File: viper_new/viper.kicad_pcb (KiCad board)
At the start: 2 copper layers, 285 x 95.1 mm, 272 parts, among them SW1 SW_Push, SW10 SW_Push, SW11 SW_Push, SW12 SW_Push, SW13 SW_Push, SW14 SW_Push, SW14_1 SW_Push, SW15 SW_Push, SW16 SW_Push, SW17 SW_Push, SW18 SW_Push, SW19 SW_Push, SW2 SW_Push, SW20 SW_Push, SW21 SW_Push, SW22 SW_Push, SW23 SW_Push, SW24 SW_Push, SW25 SW_Push, SW26 SW_Push, SW27 SW_Push, SW28 SW_Push, SW28_1 SW_Push, SW29 SW_Push, SW29_1 SW_Push, SW3 SW_Push, SW30 SW_Push, SW31 SW_Push, SW32 SW_Push, SW33 SW_Push, SW34 SW_Push, SW35 SW_Push, SW36 SW_Push, SW37 SW_Push, SW38 SW_Push, SW39 SW_Push, SW4 SW_Push, SW40 SW_Push, SW41 SW_Push, SW41_1 SW_Push, SW42 SW_Push, SW43 SW_Push, SW43_1 SW_Push, SW44 SW_Push, SW45 SW_Push, SW46 SW_Push, SW47 SW_Push, SW48 SW_Push, SW49 SW_Push, SW5 SW_Push, SW50 SW_Push, SW51 SW_Push, SW52 SW_Push, SW53 SW_Push, SW54 SW_Push, SW55 SW_Push, SW55_1 SW_Push, SW56 SW_Push, SW57 SW_Push, SW58 SW_Push, SW59 SW_Push, SW6 SW_Push, SW60 SW_Push, SW61 SW_Push, SW7 SW_Push, SW8 SW_Push, SW9 SW_Push

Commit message: YAKE - YET ANOTHER KEYBOARD EXPORT
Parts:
- D1, D10, D11, D12, D13, D14, D15, D16, D17, D18, D19, D2, D20, D21, D22, D23, D24, D25, D26, D27, D28, D29, D3, D30, D31, D32, D33, D34, D35, D36, D37, D38, D39, D4, D40, D41, D42, D43, D44, D45, D46, D47, D48, D49, D5, D50, D51, D52, D53, D54, D55, D56, D57, D58, D59, D6, D60, D61, D7, D8, D9: footprint Diode_SMD:D_SOD-123 -> Diode_SMD:D_SOD-123F
- H1: value Center Oval Mounting Hole -> Mid Viper Oval Mounting Hole; footprint acheron_MountingHoles:MoutingHole_Oval_7mm_5.0x2.5mm -> acheron_MountingHoles:Mounting_Hole_Oval_2.5x8mm
- H2: value Oval Mounting Hole -> \ Oval Mounting Hole
- H3: value Oval Mounting Hole -> Tab Oval Mounting Hole
- H4: value Mounting Hole -> G-H Mounting Hole; footprint acheron_MountingHoles:MountingHole_2.5x5.0mm -> acheron_MountingHoles:MoutingHole_Oval_BackOnly_7mm_5.0x2.5mm
- H5: value Half Side Hole -> Left Edge Half Side Hole
- H6: value Half Side Hole -> Right Edge Half Side Hole
- H7: value Oval Mounting Hole -> Space Bar Oval Mounting Hole
- H8: value Bottom Half Side Hole -> Left Bottom Half Side Hole
- H9: value Bottom Half Side Hole -> Right Bottom Half Side Hole
- R1, R10, R11, R12, R13, R14, R15, R16, R17, R18, R19, R2, R20, R21, R22, R23, R24, R25, R26, R27, R28, R29, R3, R30, R31, R32, R33, R34, R35, R36, R37, R38, R39, R4, R40, R41, R42, R43, R44, R45, R46, R47, R48, R49, R5, R50, R51, R52, R53, R54, R55, R56, R57, R58, R59, R6, R60, R61, R7, R8, R9: moved to B.Cu
- SW1, SW10, SW11, SW12, SW13, SW14_1, SW16, SW17, SW18, SW19, SW2, SW20, SW21, SW22, SW23, SW24, SW25, SW26, SW27, SW28_1, SW3, SW30, SW31, SW32, SW33, SW34, SW35, SW36, SW37, SW38, SW39, SW4, SW40, SW41_1, SW42, SW44, SW45, SW46, SW47, SW48, SW49, SW5, SW50, SW51, SW52, SW53, SW54, SW56, SW57, SW6, SW61, SW7, SW8, SW9: footprint PCM_Switch_Keyboard_Cherry_MX:SW_Cherry_MX_PCB_1.00u -> PCM_Switch_Keyboard_Hybrid:SW_Hybrid_Cherry_MX_Alps_1.00u
- SW14: footprint PCM_Switch_Keyboard_Cherry_MX:SW_Cherry_MX_PCB_1.00u -> PCM_Switch_Keyboard_Hybrid:SW_Hybrid_Cherry_MX_Alps_2.00u
- SW15, SW28, SW58, SW60: footprint PCM_Switch_Keyboard_Cherry_MX:SW_Cherry_MX_PCB_1.00u -> PCM_Switch_Keyboard_Hybrid:SW_Hybrid_Cherry_MX_Alps_1.50u
- SW29, SW55_1: footprint PCM_Switch_Keyboard_Cherry_MX:SW_Cherry_MX_PCB_1.00u -> PCM_Switch_Keyboard_Hybrid:SW_Hybrid_Cherry_MX_Alps_1.75u
- SW29_1, SW43_1: footprint PCM_Switch_Keyboard_Cherry_MX:SW_Cherry_MX_PCB_1.00u -> PCM_Switch_Keyboard_Hybrid:SW_Hybrid_Cherry_MX_Alps_1.25u
- SW41, SW43: footprint PCM_Switch_Keyboard_Cherry_MX:SW_Cherry_MX_PCB_1.00u -> PCM_Switch_Keyboard_Hybrid:SW_Hybrid_Cherry_MX_Alps_2.25u
- SW55: footprint PCM_Switch_Keyboard_Cherry_MX:SW_Cherry_MX_PCB_1.00u -> PCM_Switch_Keyboard_Hybrid:SW_Hybrid_Cherry_MX_Alps_2.75u
- SW59: footprint PCM_Switch_Keyboard_Cherry_MX:SW_Cherry_MX_PCB_1.00u -> PCM_Switch_Keyboard_Hybrid:SW_Hybrid_Cherry_MX_Alps_7.00u
- moved D25 6.23 mm to (295.3, 64.8), turned to 0 degrees
- moved D40 6.23 mm to (319.1, 83.8), turned to 0 degrees
- moved D52 6.23 mm to (271.5, 102.8), turned to 0 degrees
- moved D58 6.23 mm to (147.6, 121.9), turned to 0 degrees
- moved D59 6.23 mm to (228.6, 121.9), turned to 0 degrees
- moved D17 6.23 mm to (142.9, 64.8), turned to 0 degrees
- moved D19 6.23 mm to (181.0, 64.8), turned to 0 degrees
- moved D21 6.23 mm to (219.1, 64.8), turned to 0 degrees
- moved D22 6.23 mm to (238.1, 64.8), turned to 0 degrees
- moved D3 6.23 mm to (133.3, 45.7), turned to 0 degrees
- moved D5 6.23 mm to (171.4, 45.7), turned to 0 degrees
- moved D6 6.23 mm to (190.5, 45.7), turned to 0 degrees
- moved D8 6.23 mm to (228.6, 45.7), turned to 0 degrees
- moved D31 6.23 mm to (147.6, 83.8), turned to 0 degrees
- moved D32 6.23 mm to (166.7, 83.8), turned to 0 degrees
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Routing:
- net COL11: track 0.00 -> 118.5 mm
- net COL0: track 0.00 -> 102.0 mm
- net COL10: track 0.00 -> 82.2 mm
- net COL6: track 0.00 -> 82.2 mm
- net COL4: track 0.00 -> 82.2 mm
- net COL9: track 0.00 -> 82.2 mm
- net COL5: track 0.00 -> 82.2 mm
- net COL8: track 0.00 -> 82.2 mm
- net COL3: track 0.00 -> 82.2 mm
- net COL7: track 0.00 -> 82.2 mm
- net COL2: track 0.00 -> 82.2 mm
- net COL1: track 0.00 -> 80.4 mm
- net COL12: track 0.00 -> 57.9 mm
- net ROW2: track 0.00 -> 46.8 mm
- net COL13: track 0.00 -> 35.3 mm
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
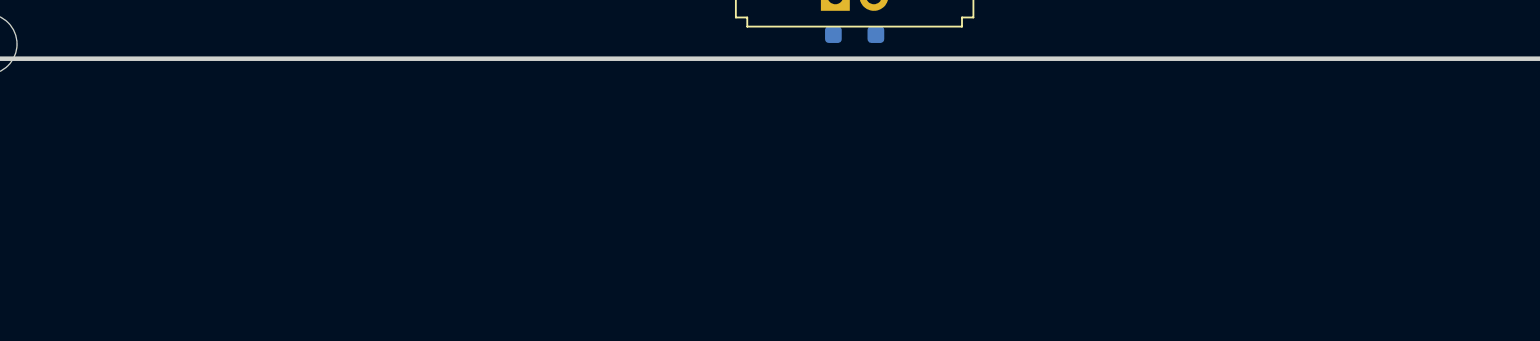
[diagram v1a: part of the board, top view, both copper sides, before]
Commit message: Added LED matrix & RGB LEDs
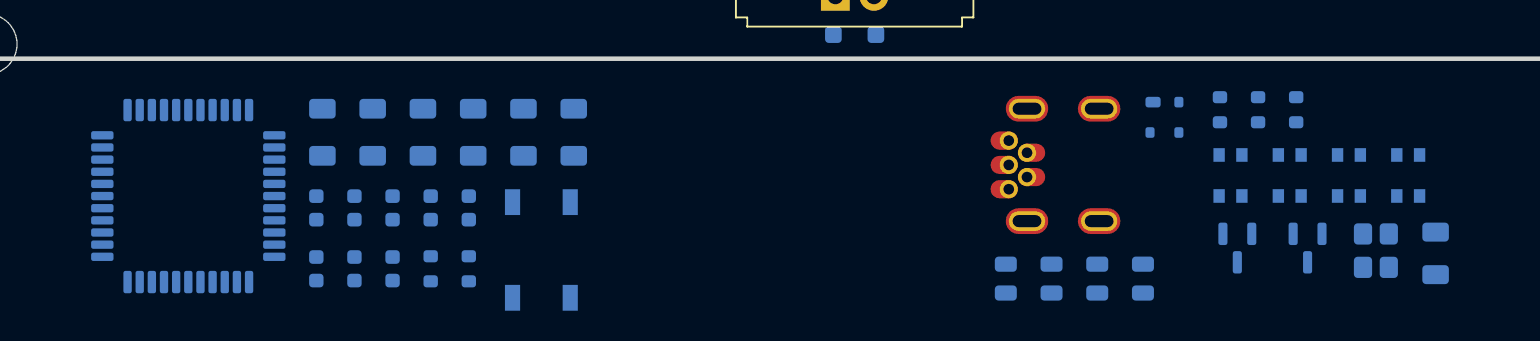
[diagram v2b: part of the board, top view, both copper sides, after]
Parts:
- added C1: 22p, Capacitor_SMD:C_0603_1608Metric, B.Cu at (193.2, 133.3)
- added C2: 22p, Capacitor_SMD:C_0603_1608Metric, B.Cu at (195.7, 133.3)
- added C3: 0.1u, Capacitor_SMD:C_0603_1608Metric, B.Cu at (198.2, 133.3)
- added C4: 0.1u, Capacitor_SMD:C_0603_1608Metric, B.Cu at (200.7, 133.3)
- added C5: 0.1u, Capacitor_SMD:C_0603_1608Metric, B.Cu at (203.2, 133.3)
- added C6: 0.1u, Capacitor_SMD:C_0603_1608Metric, B.Cu at (193.2, 137.3)
- added C7: 10u, Capacitor_SMD:C_0603_1608Metric, B.Cu at (195.7, 137.3)
- added C8: 1u, Capacitor_SMD:C_0603_1608Metric, B.Cu at (198.2, 137.3)
- added CRGB1: 100n, Capacitor_SMD:C_0805_2012Metric, B.Cu at (238.6, 138.0)
- added CRGB10: 100n, Capacitor_SMD:C_0805_2012Metric, B.Cu at (247.6, 138.0)
- added CRGB2: 100n, Capacitor_SMD:C_0805_2012Metric, B.Cu at (241.6, 138.0)
- added CRGB3: 100n, Capacitor_SMD:C_0805_2012Metric, B.Cu at (244.6, 138.0)
- added F1: Polyfuse_Small, Fuse:Fuse_1206_3216Metric, B.Cu at (266.9, 136.3)
- added J2: USB_B_Mini, acheron_Connectors:USB_MiniB_XM7D-0512, B.Cu at (239.9, 130.5)
- added Q1: 2N7002, Package_TO_SOT_SMD:SOT-23, B.Cu at (253.8, 136.0)
- added Q2: BSS138, Package_TO_SOT_SMD:SOT-23, B.Cu at (258.4, 136.0)
- added R62: 22, Resistor_SMD:R_0603_1608Metric, B.Cu at (200.7, 137.3)
- added R63: 22, Resistor_SMD:R_0603_1608Metric, B.Cu at (203.2, 137.3)
- added R64: 10k, Resistor_SMD:R_0603_1608Metric, B.Cu at (252.7, 126.8)
- added R65: 10k, Resistor_SMD:R_0603_1608Metric, B.Cu at (255.2, 126.8)
- added R66: 1k, Resistor_SMD:R_0603_1608Metric, B.Cu at (257.7, 126.8)
- added RGB1: WS2812B, locallib:LED_SMD3528-4P-WS2812B, B.Cu at (253.3, 131.2)
- added RGB10: WS2812B, locallib:LED_SMD3528-4P-WS2812B, B.Cu at (265.1, 131.2)
- added RGB2: WS2812B, locallib:LED_SMD3528-4P-WS2812B, B.Cu at (257.2, 131.2)
- added RGB3: WS2812B, locallib:LED_SMD3528-4P-WS2812B, B.Cu at (261.1, 131.2)
- added RRGB1: 5.1R, Resistor_SMD:R_1206_3216Metric_Pad1.30x1.75mm_HandSolder, B.Cu at (193.6, 128.3)
- added RRGB10: 5.1R, Resistor_SMD:R_1206_3216Metric_Pad1.30x1.75mm_HandSolder, B.Cu at (203.5, 128.3)
- added RRGB2: 5.1R, Resistor_SMD:R_1206_3216Metric_Pad1.30x1.75mm_HandSolder, B.Cu at (196.9, 128.3)
- added RRGB3: 5.1R, Resistor_SMD:R_1206_3216Metric_Pad1.30x1.75mm_HandSolder, B.Cu at (200.2, 128.3)
- added RS1: 10k, Resistor_SMD:R_1206_3216Metric_Pad1.30x1.75mm_HandSolder, B.Cu at (206.8, 128.3)
- added RS2: 10k, Resistor_SMD:R_1206_3216Metric_Pad1.30x1.75mm_HandSolder, B.Cu at (210.1, 128.3)
- added RST1: SW_SPST, Button_Switch_SMD:SW_SPST_TL3342, B.Cu at (208.0, 136.1)
- added U1: ATmega32U4-A, Package_QFP:TQFP-44_10x10mm_P0.8mm, B.Cu at (184.7, 132.5)
- added U2: PRTR5V0U2X, Package_TO_SOT_SMD:SOT-143, B.Cu at (249.0, 127.3)
- added Y1: Crystal_GND24, Crystal:Crystal_SMD_3225-4Pin_3.2x2.5mm, B.Cu at (262.9, 136.1)
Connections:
- net GND renamed LEDGND

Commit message: Placed parts with respect to SW1
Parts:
- removed CRGB10: 100n, Capacitor_SMD:C_0805_2012Metric
- removed J2: USB_B_Mini, acheron_Connectors:USB_MiniB_XM7D-0512
- removed Q2: BSS138, Package_TO_SOT_SMD:SOT-23
- removed RGB10: WS2812B, locallib:LED_SMD3528-4P-WS2812B
- removed RRGB1, RRGB10, RRGB2, RRGB3: 5.1R, Resistor_SMD:R_1206_3216Metric_Pad1.30x1.75mm_HandSolder
- removed RS1, RS2: 10k, Resistor_SMD:R_1206_3216Metric_Pad1.30x1.75mm_HandSolder
- added CRGB4: 100n, Capacitor_SMD:C_0805_2012Metric, B.Cu at (366.1, 81.7)
- added J1: USB_B_Mini, acheron_Connectors:USB_MiniB_Hirose_UX60-MB-5S8, B.Cu at (104.3, 35.8)
- added RGB4: WS2812B, locallib:LED_SMD3528-4P-WS2812B, B.Cu at (369.0, 78.3)
- LED1, LED10, LED11, LED12, LED13, LED14, LED14_1, LED15, LED16, LED17, LED18, LED19, LED2, LED20, LED21, LED22, LED23, LED24, LED25, LED26, LED27, LED28, LED28_1, LED29, LED29_1, LED3, LED30, LED31, LED32, LED33, LED34, LED35, LED36, LED37, LED38, LED39, LED4, LED40, LED41, LED41_1, LED42, LED43, LED43_1, LED44, LED45, LED46, LED47, LED48, LED49, LED5, LED50, LED51, LED52, LED53, LED54, LED55, LED55_1, LED56, LED57, LED58, LED59, LED6, LED60, LED61, LED7, LED8, LED9: value LED_Small -> LED
- moved F1 188.5 mm to (101.2, 46.4)
- moved RGB1 181.1 mm to (88.2, 56.8)
- moved RGB3 180.9 mm to (88.2, 78.3), turned to 90 degrees
- moved CRGB1 171.4 mm to (88.7, 54.9), turned to 180 degrees
- moved U2 168.1 mm to (104.8, 41.1), turned to 180 degrees
- moved CRGB3 167.8 mm to (88.4, 76.5), turned to 0 degrees
- moved CRGB2 151.5 mm to (367.9, 54.4), turned to 180 degrees
- moved RGB2 134.2 mm to (369.0, 56.8)
- moved C7 131.9 mm to (96.2, 50.7), turned to 180 degrees
- moved RST1 109.9 mm to (115.2, 77.1)
- moved R64 87.4 mm to (166.1, 115.4), turned to 180 degrees
- moved Y1 70.8 mm to (195.4, 114.9)
- moved R66 63.9 mm to (197.5, 105.2), turned to 0 degrees
- moved R65 60.6 mm to (197.5, 108.2), turned to 180 degrees
- moved Q1 58.2 mm to (203.6, 106.4), turned to 180 degrees
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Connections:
- C3 pad 1: +5V -> VCC
- C4 pad 1: +5V -> VCC
- C5 pad 1: +5V -> VCC
- C6 pad 1: +5V -> VCC
- C7 pad 1: +5V -> VCC
- CRGB1 pad 1: Net-(RGB1-VDD) -> VCC
- CRGB2 pad 1: Net-(RGB2-VDD) -> VCC
- CRGB3 pad 1: Net-(RGB3-VDD) -> VCC
- F1 pad 1: +5V -> VCC
- F1 pad 2: VCC -> +5V
- LED1 pad 2: LEDGND -> LED_GND
- LED10 pad 2: LEDGND -> LED_GND
- LED11 pad 2: LEDGND -> LED_GND
- LED12 pad 2: LEDGND -> LED_GND
- LED13 pad 2: LEDGND -> LED_GND
- LED14 pad 2: LEDGND -> LED_GND
- LED14_1 pad 2: LEDGND -> LED_GND
- LED15 pad 2: LEDGND -> LED_GND
- LED16 pad 2: LEDGND -> LED_GND
- LED17 pad 2: LEDGND -> LED_GND
- LED18 pad 2: LEDGND -> LED_GND
- LED19 pad 2: LEDGND -> LED_GND
- LED2 pad 2: LEDGND -> LED_GND
- LED20 pad 2: LEDGND -> LED_GND
- LED21 pad 2: LEDGND -> LED_GND
- LED22 pad 2: LEDGND -> LED_GND
- LED23 pad 2: LEDGND -> LED_GND
- LED24 pad 2: LEDGND -> LED_GND
- LED25 pad 2: LEDGND -> LED_GND
- LED26 pad 2: LEDGND -> LED_GND
- LED27 pad 2: LEDGND -> LED_GND
- LED28 pad 2: LEDGND -> LED_GND
- LED28_1 pad 2: LEDGND -> LED_GND
- LED29 pad 2: LEDGND -> CAPS_LED
- LED29_1 pad 2: LEDGND -> CAPS_LED
- LED3 pad 2: LEDGND -> LED_GND
- LED30 pad 2: LEDGND -> LED_GND
- LED31 pad 2: LEDGND -> LED_GND
- LED32 pad 2: LEDGND -> LED_GND
- LED33 pad 2: LEDGND -> LED_GND
- LED34 pad 2: LEDGND -> LED_GND
- LED35 pad 2: LEDGND -> LED_GND
- LED36 pad 2: LEDGND -> LED_GND
- LED37 pad 2: LEDGND -> LED_GND
- LED38 pad 2: LEDGND -> LED_GND
- LED39 pad 2: LEDGND -> LED_GND
- LED4 pad 2: LEDGND -> LED_GND
- LED40 pad 2: LEDGND -> LED_GND
- LED41 pad 2: LEDGND -> LED_GND
- LED41_1 pad 2: LEDGND -> LED_GND
- LED42 pad 2: LEDGND -> LED_GND
- LED43 pad 2: LEDGND -> LED_GND
- LED43_1 pad 2: LEDGND -> LED_GND
- LED44 pad 2: LEDGND -> LED_GND
- LED45 pad 2: LEDGND -> LED_GND
- LED46 pad 2: LEDGND -> LED_GND
- LED47 pad 2: LEDGND -> LED_GND
- LED48 pad 2: LEDGND -> LED_GND
- LED49 pad 2: LEDGND -> LED_GND
- LED5 pad 2: LEDGND -> LED_GND
- LED50 pad 2: LEDGND -> LED_GND
- LED51 pad 2: LEDGND -> LED_GND
- LED52 pad 2: LEDGND -> LED_GND
- LED53 pad 2: LEDGND -> LED_GND
- LED54 pad 2: LEDGND -> LED_GND
- LED55 pad 2: LEDGND -> LED_GND
- LED55_1 pad 2: LEDGND -> LED_GND
- LED56 pad 2: LEDGND -> LED_GND
- LED57 pad 2: LEDGND -> LED_GND
- LED58 pad 2: LEDGND -> LED_GND
- LED59 pad 2: LEDGND -> LED_GND
- LED6 pad 2: LEDGND -> LED_GND
- LED60 pad 2: LEDGND -> LED_GND
- LED61 pad 2: LEDGND -> LED_GND
- LED7 pad 2: LEDGND -> LED_GND
- LED8 pad 2: LEDGND -> LED_GND
- LED9 pad 2: LEDGND -> LED_GND
- Q1 pad 3: LEDGND -> LED_GND
- R1 pad 1: +5V -> VCC
- R10 pad 1: +5V -> VCC
- R11 pad 1: +5V -> VCC
- R12 pad 1: +5V -> VCC
- R13 pad 1: +5V -> VCC
- R14 pad 1: +5V -> VCC
- R15 pad 1: +5V -> VCC
- R16 pad 1: +5V -> VCC
- R17 pad 1: +5V -> VCC
- R18 pad 1: +5V -> VCC
- R19 pad 1: +5V -> VCC
- R2 pad 1: +5V -> VCC
- R20 pad 1: +5V -> VCC
- R21 pad 1: +5V -> VCC
- R22 pad 1: +5V -> VCC
- R23 pad 1: +5V -> VCC
- R24 pad 1: +5V -> VCC
- R25 pad 1: +5V -> VCC
- R26 pad 1: +5V -> VCC
- R27 pad 1: +5V -> VCC
- R28 pad 1: +5V -> VCC
- R29 pad 1: +5V -> VCC
- R3 pad 1: +5V -> VCC
- R30 pad 1: +5V -> VCC
- R31 pad 1: +5V -> VCC
- R32 pad 1: +5V -> VCC
- R33 pad 1: +5V -> VCC
- R34 pad 1: +5V -> VCC
- R35 pad 1: +5V -> VCC
- R36 pad 1: +5V -> VCC
- R37 pad 1: +5V -> VCC
- R38 pad 1: +5V -> VCC
- R39 pad 1: +5V -> VCC
- R4 pad 1: +5V -> VCC
- R40 pad 1: +5V -> VCC
- R41 pad 1: +5V -> VCC
- R42 pad 1: +5V -> VCC
- R43 pad 1: +5V -> VCC
- R44 pad 1: +5V -> VCC
- R45 pad 1: +5V -> VCC
- R46 pad 1: +5V -> VCC
- R47 pad 1: +5V -> VCC
- R48 pad 1: +5V -> VCC
- R49 pad 1: +5V -> VCC
- R5 pad 1: +5V -> VCC
- R50 pad 1: +5V -> VCC
- R51 pad 1: +5V -> VCC
- R52 pad 1: +5V -> VCC
- R53 pad 1: +5V -> VCC
- R54 pad 1: +5V -> VCC
- R55 pad 1: +5V -> VCC
- R56 pad 1: +5V -> VCC
- R57 pad 1: +5V -> VCC
- R58 pad 1: +5V -> VCC
- R59 pad 1: +5V -> VCC
- R6 pad 1: +5V -> VCC
- R60 pad 1: +5V -> VCC
- R61 pad 1: +5V -> VCC
- R65 pad 2: +5V -> VCC
- R66 pad 1: Net-(Q1-G) -> Net-(U1-PB7)
- R66 pad 2: Net-(U1-PB7) -> Net-(Q1-G)
- R7 pad 1: +5V -> VCC
- R8 pad 1: +5V -> VCC
- R9 pad 1: +5V -> VCC
- RGB1 pad 1: Net-(RGB1-VDD) -> VCC
- RGB1 pad 4: RGB_5V -> RGB_LED
- RGB2 pad 1: Net-(RGB2-VDD) -> VCC
- RGB3 pad 1: Net-(RGB3-VDD) -> VCC
- U1 pad 14: +5V -> VCC
- U1 pad 2: +5V -> VCC
- U1 pad 24: +5V -> VCC
- U1 pad 34: +5V -> VCC
- U1 pad 36: unconnected-(U1-PF7-Pad36) -> RGB_LED
- U1 pad 44: +5V -> VCC
- U1 pad 7: +5V -> VCC
- U1 pad 8: unconnected-(U1-PB0-Pad8) -> CAPS_LED
- U2 pad 4: VCC -> +5V
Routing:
- net COL11: track 118.5 -> 0.00 mm
- net COL0: track 102.0 -> 0.00 mm
- net COL10: track 82.2 -> 0.00 mm
- net COL6: track 82.2 -> 0.00 mm
- net COL4: track 82.2 -> 0.00 mm
- net COL9: track 82.2 -> 0.00 mm
- net COL5: track 82.2 -> 0.00 mm
- net COL8: track 82.2 -> 0.00 mm
- net COL3: track 82.2 -> 0.00 mm
- net COL7: track 82.2 -> 0.00 mm
- net COL2: track 82.2 -> 0.00 mm
- net COL1: track 80.4 -> 0.00 mm
- net COL12: track 57.9 -> 0.00 mm
- net ROW2: track 46.8 -> 0.00 mm
- net COL13: track 35.3 -> 0.00 mm

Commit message: and the story continues
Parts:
- removed ST28_1: ISO Enter Stabilizer, PCM_Mounting_Keyboard_Stabilizer:Stabilizer_Cherry_MX_2.00u
- removed SW28_1: SW_Push, PCM_Switch_Keyboard_Hybrid:SW_Hybrid_Cherry_MX_Alps_1.00u
- turned ST41 to 180 degrees
- turned ST43 to 180 degrees
- turned ST55 to 180 degrees
- turned ST59 to 180 degrees
